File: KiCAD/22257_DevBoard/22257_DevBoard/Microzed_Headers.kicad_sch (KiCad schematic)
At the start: 4 parts, among them J1 TD-120-G-AACON40_2X20_TU_HTS_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, J2 TD-120-G-AACON40_2X20_TU_HTS_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

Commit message: EOD
Nearly finished routing
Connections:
- net 3V3 renamed +3.3V
- net 5V renamed +5V

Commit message: DONE ROUTINGgit add .git add .
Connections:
- net 35_L15 renamed BRD_10MHz_IN
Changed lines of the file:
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@@
 	)
 	(junction
-		(at 104.14 101.6)
+		(at 93.98 101.6)
 		(diameter 0)
 		(color 0 0 0 0)
@@
 	)
 	(junction
-		(at 104.14 190.5)
+		(at 93.98 190.5)
 		(diameter 0)
 		(color 0 0 0 0)
@@
 	)
 	(junction
-		(at 104.14 165.1)
+		(at 93.98 165.1)
 		(diameter 0)
 		(color 0 0 0 0)
@@
 	)
 	(junction
-		(at 104.14 124.46)
+		(at 93.98 124.46)
 		(diameter 0)
 		(color 0 0 0 0)
@@
 	)
 	(junction
-		(at 104.14 139.7)
+		(at 93.98 139.7)
 		(diameter 0)
 		(color 0 0 0 0)
@@
 	)
 	(junction
-		(at 104.14 157.48)
+		(at 93.98 157.48)
 		(diameter 0)
 		(color 0 0 0 0)
@@
 	)
 	(junction
-		(at 104.14 109.22)
+		(at 93.98 109.22)
 		(diameter 0)
 		(color 0 0 0 0)
@@
 	)
 	(junction
-		(at 104.14 132.08)
+		(at 93.98 132.08)
 		(diameter 0)
 		(color 0 0 0 0)
@@
 	)
 	(junction
-		(at 104.14 182.88)
+		(at 93.98 182.88)
 		(diameter 0)
 		(color 0 0 0 0)
 	)
 	(junction
-		(at 104.14 116.84)
+		(at 93.98 116.84)
 		(diameter 0)
 		(color 0 0 0 0)
@@
 	(wire
 		(pts
-			(xy 104.14 165.1) (xy 104.14 182.88)
+			(xy 93.98 165.1) (xy 93.98 182.88)
 		)
 		(stroke
@@
 	(wire
 		(pts
-			(xy 104.14 157.48) (xy 125.73 157.48)
+			(xy 93.98 157.48) (xy 125.73 157.48)
 		)
 		(stroke
@@
 	(wire
 		(pts
-			(xy 104.14 101.6) (xy 125.73 101.6)
+			(xy 93.98 101.6) (xy 125.73 101.6)
 		)
 		(stroke
@@
 	(wire
 		(pts
-			(xy 104.14 165.1) (xy 125.73 165.1)
+			(xy 93.98 165.1) (xy 125.73 165.1)
 		)
 		(stroke
@@
 	(wire
 		(pts
-			(xy 104.14 101.6) (xy 104.14 109.22)
+			(xy 93.98 101.6) (xy 93.98 109.22)
 		)
 		(stroke
@@
 	(wire
 		(pts
-			(xy 104.14 190.5) (xy 104.14 194.31)
+			(xy 93.98 190.5) (xy 93.98 194.31)
 		)
 		(stroke
@@
 	(wire
 		(pts
-			(xy 104.14 182.88) (xy 104.14 190.5)
+			(xy 93.98 182.88) (xy 93.98 190.5)
 		)
 		(stroke
@@
 	(wire
 		(pts
-			(xy 104.14 116.84) (xy 125.73 116.84)
+			(xy 93.98 116.84) (xy 125.73 116.84)
 		)
 		(stroke
@@
 	(wire
 		(pts
-			(xy 104.14 157.48) (xy 104.14 165.1)
+			(xy 93.98 157.48) (xy 93.98 165.1)
 		)
 		(stroke
@@
 	(wire
 		(pts
-			(xy 104.14 116.84) (xy 104.14 124.46)
+			(xy 93.98 116.84) (xy 93.98 124.46)
 		)
 		(stroke
@@
 	(wire
 		(pts
-			(xy 104.14 139.7) (xy 104.14 157.48)
+			(xy 93.98 139.7) (xy 93.98 157.48)
 		)
 		(stroke
@@
 	(wire
 		(pts
-			(xy 104.14 109.22) (xy 125.73 109.22)
+			(xy 93.98 109.22) (xy 125.73 109.22)
 		)
 		(stroke
@@
 	(wire
 		(pts
-			(xy 104.14 132.08) (xy 104.14 139.7)
+			(xy 93.98 132.08) (xy 93.98 139.7)
 		)
 		(stroke
@@
 	(wire
 		(pts
-			(xy 104.14 190.5) (xy 125.73 190.5)
+			(xy 93.98 190.5) (xy 125.73 190.5)
 		)
 		(stroke
@@
 	(wire
 		(pts
-			(xy 104.14 124.46) (xy 125.73 124.46)
+			(xy 93.98 124.46) (xy 125.73 124.46)
 		)
 		(stroke
@@
 	(wire
 		(pts
-			(xy 104.14 132.08) (xy 125.73 132.08)
+			(xy 93.98 132.08) (xy 125.73 132.08)
 		)
 		(stroke
@@
 	(wire
 		(pts
-			(xy 104.14 124.46) (xy 104.14 132.08)
+			(xy 93.98 124.46) (xy 93.98 132.08)
 		)
 		(stroke
@@
 	(wire
 		(pts
-			(xy 104.14 109.22) (xy 104.14 116.84)
+			(xy 93.98 109.22) (xy 93.98 116.84)
 		)
 		(stroke
@@
 	(wire
 		(pts
-			(xy 104.14 139.7) (xy 125.73 139.7)
+			(xy 93.98 139.7) (xy 125.73 139.7)
 		)
 		(stroke
@@
 	(wire
 		(pts
-			(xy 104.14 93.98) (xy 104.14 101.6)
+			(xy 93.98 93.98) (xy 93.98 101.6)
 		)
 		(stroke
@@
 	(wire
 		(pts
-			(xy 104.14 93.98) (xy 125.73 93.98)
+			(xy 93.98 93.98) (xy 125.73 93.98)
 		)
 		(stroke
@@
 	(wire
 		(pts
-			(xy 104.14 182.88) (xy 125.73 182.88)
+			(xy 93.98 182.88) (xy 125.73 182.88)
 		)
 		(stroke
@@
 		)
 	)
+	(global_label "BRD_10MHz_IN"
+		(shape input)
+		(at 114.3 180.34 180)
+		(fields_autoplaced yes)
+		(effects
+			(font
+				(size 1.27 1.27)
+			)
+			(justify right)
+		)
+		(property "Intersheetrefs" "${INTERSHEET_REFS}"
+			(at 97.4053 180.34 0)
+			(effects
+				(font
+					(size 1.27 1.27)
+				)
+				(justify right)
+				(hide yes)
+			)
+		)
+	)
 	(global_label "TCXO_OE"
 		(shape output)
@@
 	(symbol
 		(lib_id "ZED_BREAKOUT_v22-eagle-import:GND")
-		(at 104.14 196.85 0)
+		(at 93.98 196.85 0)
 		(unit 1)
 		(exclude_from_sim no)
@@
 		(dnp no)
 		(property "Reference" "#SUPPLY0105"
-			(at 104.14 196.85 0)
+			(at 93.98 196.85 0)
 			(effects
 				(font
@@
 		)
 		(property "Value" "GND"
-			(at 102.235 200.025 0)
+			(at 92.075 200.025 0)
 			(effects
 				(font
@@
 		)
 		(property "Footprint" ""
-			(at 104.14 196.85 0)
+			(at 93.98 196.85 0)
 			(effects
 				(font
@@
 		)
 		(property "Datasheet" ""
-			(at 104.14 196.85 0)
+			(at 93.98 196.85 0)
 			(effects
 				(font
@@
 		)
 		(property "Description" ""
-			(at 104.14 196.85 0)
+			(at 93.98 196.85 0)
 			(effects
 				(font

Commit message: Added notes from review with Carlos
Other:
- note added: "50 OHM RESISTORS FOR DRIVING SIDE OF SPI LINES"
- note added: "EXTERNAL 10K PULLUPS FOR I2C LINES"
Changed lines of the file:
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@@
 	(generator_version "9.0")
 	(paper "A3")
+	(text "EXTERNAL 10K PULLUPS FOR I2C LINES"
+		(exclude_from_sim no)
+		(at 207.518 63.5 0)
+		(effects
+			(font
+				(size 5.08 5.08)
+				(color 255 22 0 1)
+			)
+		)
+	)
 	(text "MicroZed Headers"
 		(exclude_from_sim no)
@@
 		)
 	)
+	(text "50 OHM RESISTORS FOR\nDRIVING SIDE OF SPI LINES"
+		(exclude_from_sim no)
+		(at 315.214 128.524 0)
+		(effects
+			(font
+				(size 5.08 5.08)
+				(color 255 22 0 1)
+			)
+		)
+	)
 	(junction
 		(at 93.98 101.6)
@@
 	(wire
 		(pts
-			(xy 374.65 182.88) (xy 374.65 186.69)
-		)
-		(stroke
-			(width 0)
-			(type default)
-		)
-	)
-	(wire
-		(pts
 			(xy 379.73 142.24) (xy 374.65 142.24)
 		)
@@
 	(wire
 		(pts
+			(xy 218.44 200.66) (xy 218.44 203.2)
+		)
+		(stroke
+			(width 0)
+			(type default)
+		)
+	)
+	(wire
+		(pts
+			(xy 374.65 182.88) (xy 374.65 189.23)
+		)
+		(stroke
+			(width 0)
+			(type default)
+		)
+	)
+	(wire
+		(pts
 			(xy 119.38 119.38) (xy 125.73 119.38)
 		)
@@
 	(wire
 		(pts
+			(xy 328.93 200.66) (xy 328.93 203.2)
+		)
+		(stroke
+			(width 0)
+			(type default)
+		)
+	)
+	(wire
+		(pts
 			(xy 171.45 91.44) (xy 184.15 91.44)
 		)
@@
 	)
 	(symbol
-		(lib_id "ZED_BREAKOUT_v22-eagle-import:GND")
+		(lib_id "power:GND")
 		(at 374.65 189.23 0)
 		(unit 1)
@@
 		)
 		(property "Value" "GND"
-			(at 372.745 192.405 0)
+			(at 372.618 194.056 0)
 			(effects
 				(font
@@
 			)
 		)
-		(property "Description" ""
+		(property "Description" "Power symbol creates a global label with name \"GND\" , ground"
 			(at 374.65 189.23 0)
 			(effects
@@
 	)
 	(symbol
-		(lib_id "ZED_BREAKOUT_v22-eagle-import:GND")
+		(lib_id "power:GND")
 		(at 328.93 203.2 0)
 		(unit 1)
@@
 		)
 		(property "Value" "GND"
-			(at 327.025 206.375 0)
+			(at 326.39 208.026 0)
 			(effects
 				(font
@@
 			)
 		)
-		(property "Description" ""
+		(property "Description" "Power symbol creates a global label with name \"GND\" , ground"
 			(at 328.93 203.2 0)
 			(effects
@@
 	)
 	(symbol
-		(lib_id "ZED_BREAKOUT_v22-eagle-import:GND")
-		(at 71.12 93.98 0)
+		(lib_id "power:GND")
+		(at 71.12 91.44 0)
 		(unit 1)
 		(exclude_from_sim no)
@@
 		(dnp no)
 		(property "Reference" "#SUPPLY04"
-			(at 71.12 93.98 0)
+			(at 71.12 91.44 0)
 			(effects
 				(font
@@
 		)
 		(property "Value" "GND"
-			(at 69.215 97.155 0)
+			(at 69.215 94.615 0)
 			(effects
 				(font
@@
 		)
 		(property "Footprint" ""
-			(at 71.12 93.98 0)
+			(at 71.12 91.44 0)
 			(effects
 				(font
@@
 		)
 		(property "Datasheet" ""
-			(at 71.12 93.98 0)
+			(at 71.12 91.44 0)
 			(effects
 				(font
@@
 			)
 		)
-		(property "Description" ""
-			(at 71.12 93.98 0)
+		(property "Description" "Power symbol creates a global label with name \"GND\" , ground"
+			(at 71.12 91.44 0)
 			(effects
 				(font
@@
 	)
 	(symbol
-		(lib_id "ZED_BREAKOUT_v22-eagle-import:GND")
-		(at 93.98 196.85 0)
+		(lib_id "power:GND")
+		(at 93.98 194.31 0)
 		(unit 1)
 		(exclude_from_sim no)
@@
 		(dnp no)
 		(property "Reference" "#SUPPLY0105"
-			(at 93.98 196.85 0)
+			(at 93.98 194.31 0)
 			(effects
 				(font
@@
 		)
 		(property "Value" "GND"
-			(at 92.075 200.025 0)
+			(at 91.44 199.136 0)
 			(effects
 				(font
@@
 		)
 		(property "Footprint" ""
-			(at 93.98 196.85 0)
+			(at 93.98 194.31 0)
 			(effects
 				(font
@@
 		)
 		(property "Datasheet" ""
-			(at 93.98 196.85 0)
+			(at 93.98 194.31 0)
 			(effects
 				(font
@@
 			)
 		)
-		(property "Description" ""
-			(at 93.98 196.85 0)
+		(property "Description" "Power symbol creates a global label with name \"GND\" , ground"
+			(at 93.98 194.31 0)
 			(effects
 				(font
@@
 	)
 	(symbol
-		(lib_id "ZED_BREAKOUT_v22-eagle-import:GND")
-		(at 53.34 193.04 0)
+		(lib_id "power:GND")
+		(at 53.34 190.5 0)
 		(unit 1)
 		(exclude_from_sim no)
@@
 		(dnp no)
 		(property "Reference" "#SUPPLY05"
-			(at 53.34 193.04 0)
+			(at 53.34 190.5 0)
 			(effects
 				(font
@@
 		)
 		(property "Value" "GND"
-			(at 51.435 196.215 0)
+			(at 51.054 195.58 0)
 			(effects
 				(font
@@
 		)
 		(property "Footprint" ""
-			(at 53.34 193.04 0)
+			(at 53.34 190.5 0)
 			(effects
 				(font
@@
 		)
 		(property "Datasheet" ""
-			(at 53.34 193.04 0)
+			(at 53.34 190.5 0)
 			(effects
 				(font
@@
 			)
 		)
-		(property "Description" ""
-			(at 53.34 193.04 0)
+		(property "Description" "Power symbol creates a global label with name \"GND\" , ground"
+			(at 53.34 190.5 0)
 			(effects
 				(font
@@
 	)
 	(symbol
-		(lib_id "ZED_BREAKOUT_v22-eagle-import:GND")
+		(lib_id "power:GND")
 		(at 218.44 203.2 0)
 		(unit 1)
@@
 		)
 		(property "Value" "GND"
-			(at 216.535 206.375 0)
+			(at 216.154 208.28 0)
 			(effects
 				(font
@@
 			)
 		)
-		(property "Description" ""
+		(property "Description" "Power symbol creates a global label with name \"GND\" , ground"
 			(at 218.44 203.2 0)
 			(effects

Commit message: Started BOM
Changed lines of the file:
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@@
 	(text "50 OHM RESISTORS FOR\nDRIVING SIDE OF SPI LINES"
 		(exclude_from_sim no)
-		(at 315.214 128.524 0)
+		(at 311.912 132.08 0)
 		(effects
 			(font

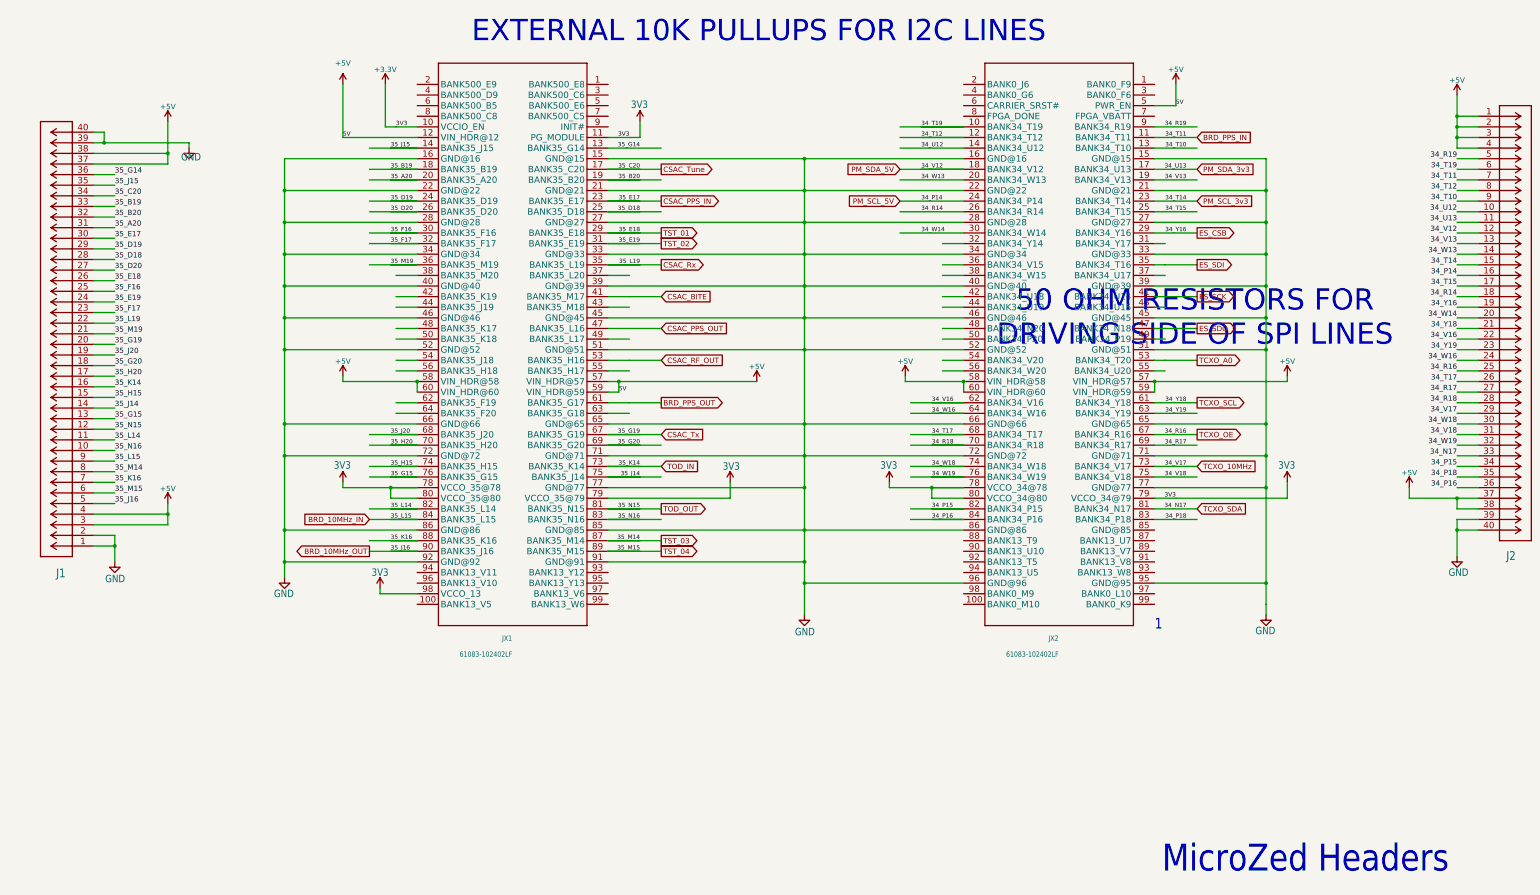
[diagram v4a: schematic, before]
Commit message: Finished Edits
Edits from design review are done, and the BOM has part numbers filled out
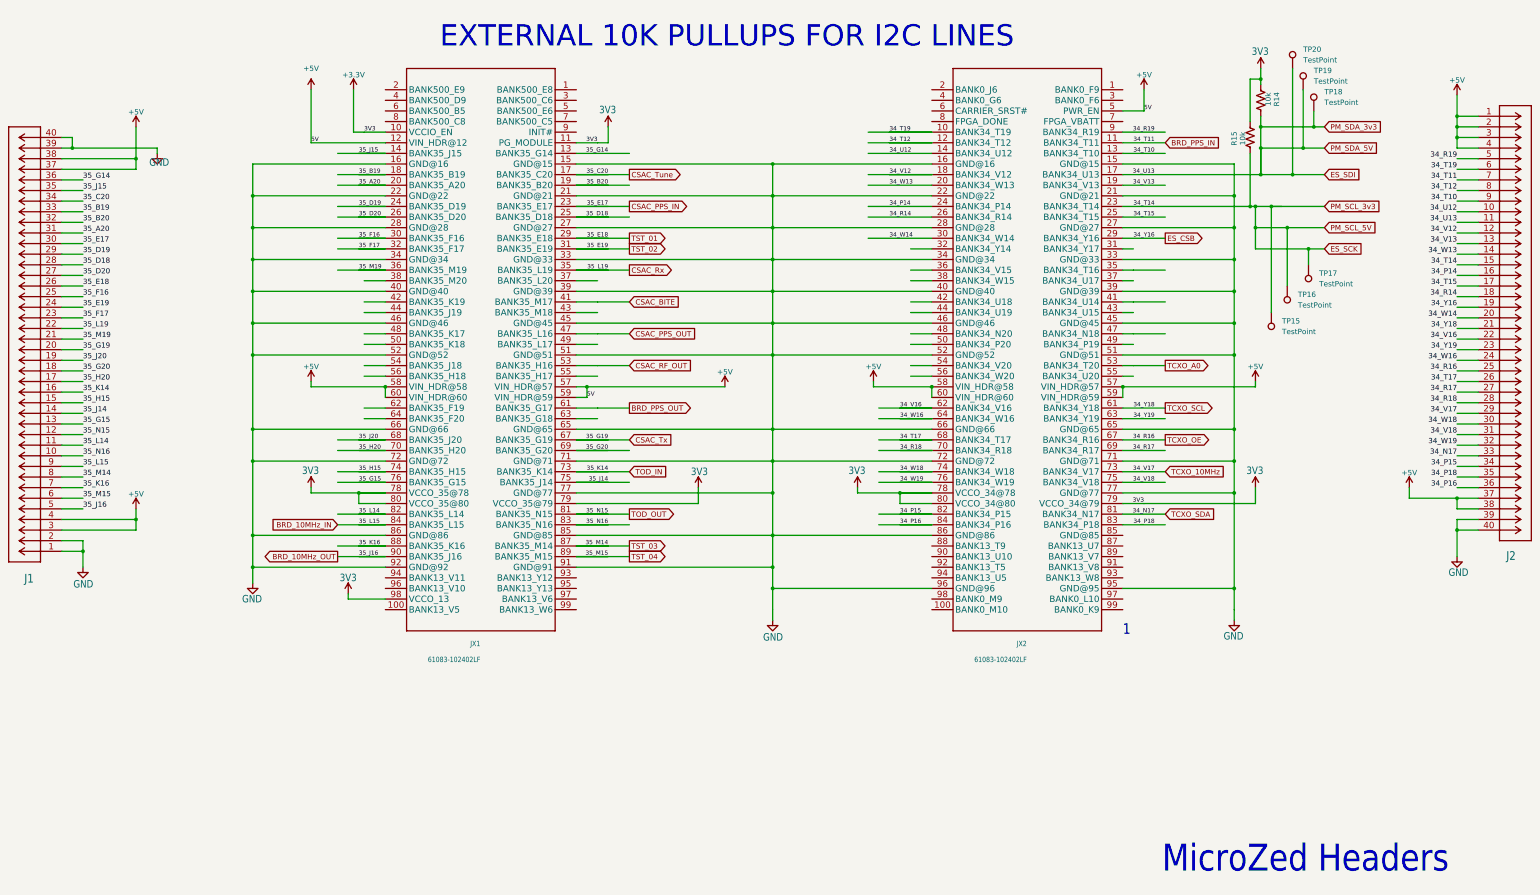
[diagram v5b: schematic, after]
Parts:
- added R14, R15: 10k, Resistor_SMD:R_0603_1608Metric, symbol Device:R_US
- added TP15, TP16, TP17, TP18, TP19, TP20: TestPoint, TestPoint:TestPoint_THTPad_2.5x2.5mm_Drill1.2mm, symbol Connector:TestPoint
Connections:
- net PM_SCL_3v3 is gone; now on net ES_SCK: J2.15, JX2.23 (BANK34_T14)
- net PM_SDA_3v3 is gone; now on net ES_SDI: J2.11, JX2.17 (BANK34_U13)
- net +3.3V: now also R14.2, R15.1
- net ES_SCK: now also R15.2, TP15.1, TP16.1, TP17.1; no longer JX2.41 (BANK34_U14)
- net ES_SDI: now also R14.1, TP18.1, TP19.1, TP20.1; no longer JX2.35 (BANK34_T16)
- net ES_SDO: no longer names the net of JX2.47 (BANK34_N18)
- net PM_SCL_5V renamed 34_P14
- net PM_SDA_5V renamed 34_V12
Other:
- note removed: "50 OHM RESISTORS FOR DRIVING SIDE OF SPI LINES"
- moved on the sheet: J1, JX1, JX2

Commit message: Output Files Generated
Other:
- note removed: "EXTERNAL 10K PULLUPS FOR I2C LINES"
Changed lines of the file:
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@@
 	(generator_version "9.0")
 	(paper "A3")
-	(text "EXTERNAL 10K PULLUPS FOR I2C LINES"
-		(exclude_from_sim no)
-		(at 199.898 64.77 0)
-		(effects
-			(font
-				(size 5.08 5.08)
-				(color 255 22 0 1)
-			)
-		)
-	)
 	(text "MicroZed Headers"
 		(exclude_from_sim no)
